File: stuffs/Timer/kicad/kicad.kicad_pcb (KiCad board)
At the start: 2 copper layers, 8 parts, among them SW1 SW_PUSH, SW2 SW_PUSH

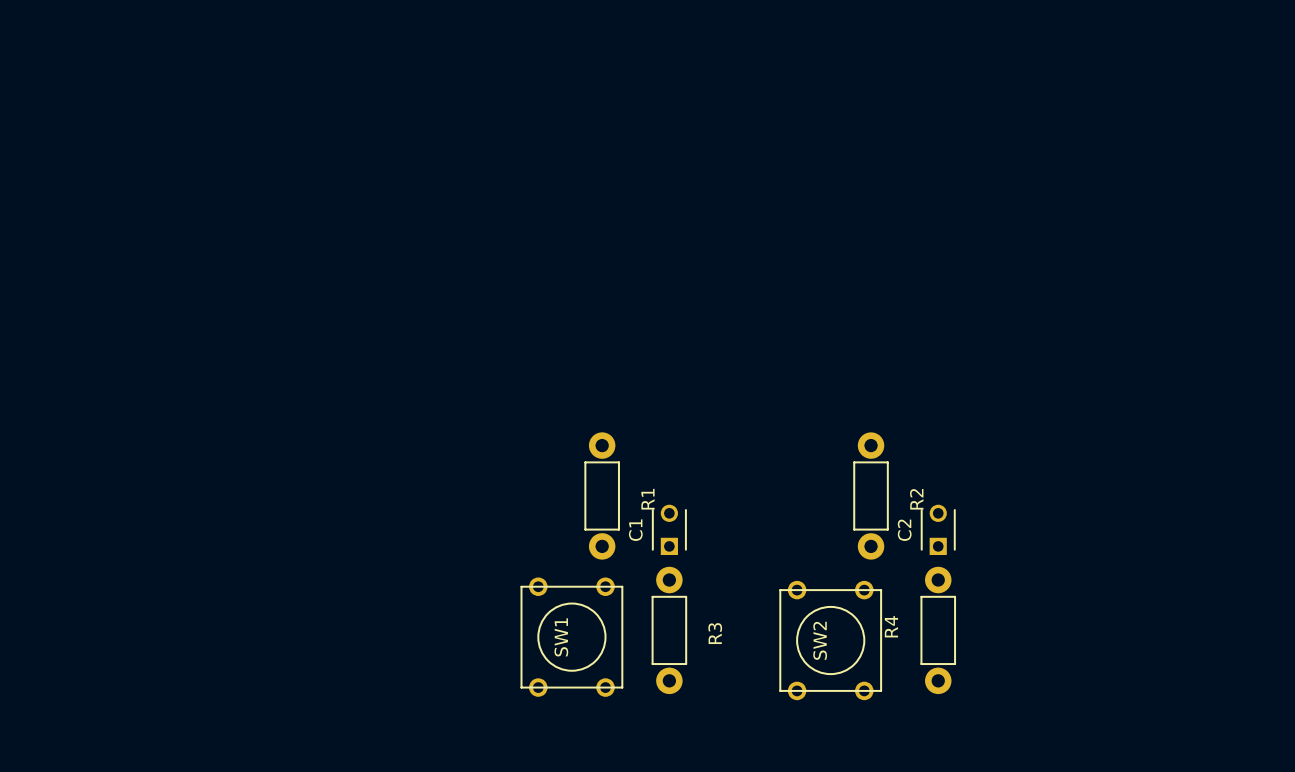
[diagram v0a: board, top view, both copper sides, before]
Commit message: Update kicad files for Timer project.
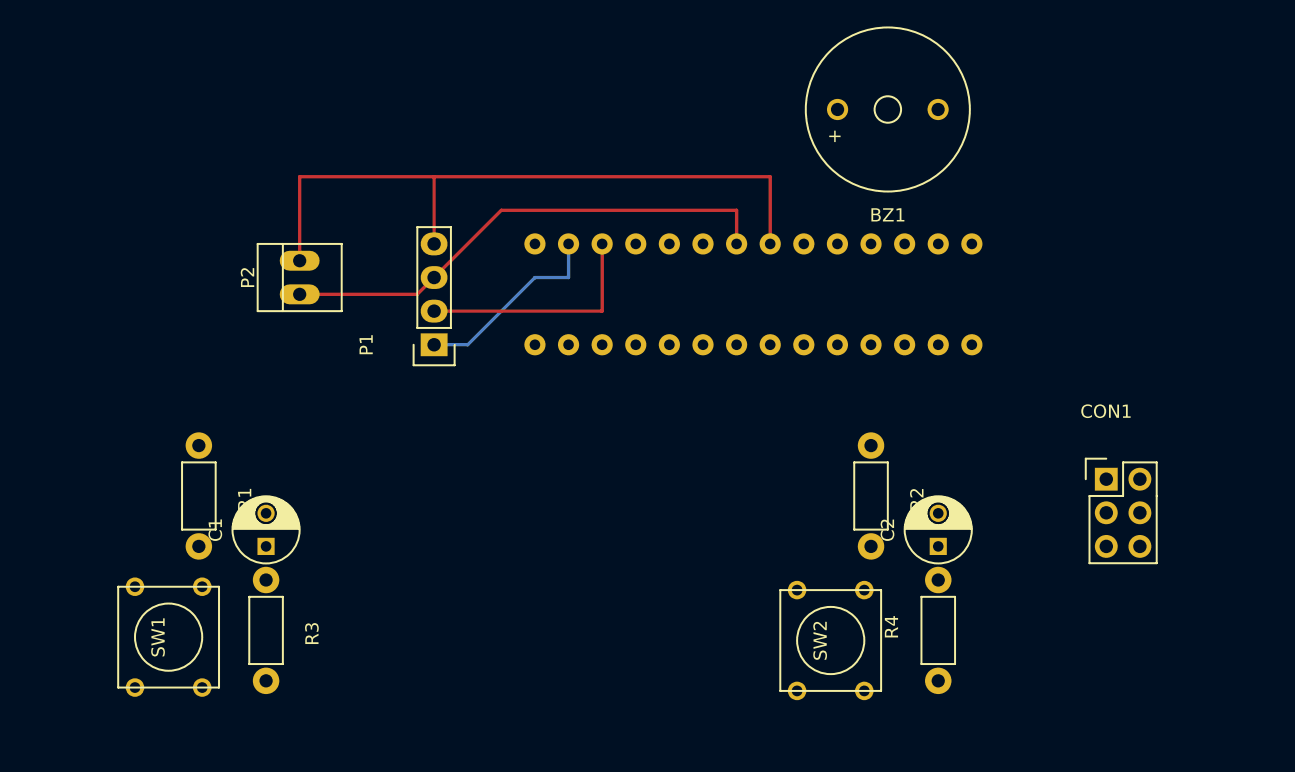
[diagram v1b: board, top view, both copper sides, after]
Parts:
- added BZ1: buzzer, Buzzers_Beepers:MagneticBuzzer_ProSignal_ABI-009-RC, F.Cu at (142.2, 38.1)
- added CON1: AVR-ISP-6, Pin_Headers:Pin_Header_Straight_2x03, F.Cu at (154.9, 66.0)
- added IC1: ATMEGA328P-P, Housings_DIP:DIP-28_W7.62mm, B.Cu at (111.8, 48.3)
- added P1: CONN_01X04, Socket_Strips:Socket_Strip_Straight_1x04, F.Cu at (104.1, 55.9)
- added P2: CONN_01X02, Connect:PINHEAD1-2, F.Cu at (94.0, 50.8)
- C1, C2: footprint Capacitors_ThroughHole:C_Disc_D3_P2.5 -> Capacitors_ThroughHole:C_Radial_D5_L6_P2.5
- moved C1 30.5 mm to (91.4, 71.1)
- moved R1 30.5 mm to (86.4, 63.5)
- moved R3 30.5 mm to (91.4, 73.7)
- moved SW1 30.5 mm to (84.1, 78.0)
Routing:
- net GND: track 0.00 -> 52.1 mm
- net VCC: track 0.00 -> 38.2 mm
- net DISPLAY_IO: track 0.00 -> 17.8 mm
- net DISPLAY_CLK: track 0.00 -> 14.8 mm

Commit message: Update kicad design files.
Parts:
- added C3: 10uF, Capacitors_ThroughHole:C_Radial_D5_L6_P2.5, F.Cu at (121.4, 70.6)
- added R5: 10, Resistors_ThroughHole:Resistor_Horizontal_RM7mm, F.Cu at (115.8, 63.8)
- added R6: 1K, Resistors_ThroughHole:Resistor_Horizontal_RM7mm, F.Cu at (121.4, 73.9)
- added SW3: SW_PUSH, Buttons_Switches_ThroughHole:SW_PUSH_SMALL, F.Cu at (113.3, 77.7)
- C1, R3: moved to B.Cu
- moved BZ1 18.7 mm to (158.0, 48.3), turned to 270 degrees
- moved R4 6.86 mm to (142.2, 74.4), turned to 270 degrees
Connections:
- IC1 pad 11: Net-(IC1-Pad11) -> INCREASE
- IC1 pad 12: Net-(IC1-Pad12) -> DECREASE
- IC1 pad 2: DISPLAY_CLK -> Net-(IC1-Pad2)
- IC1 pad 3: DISPLAY_IO -> Net-(IC1-Pad3)
- IC1 pad 4: PLAY -> DISPLAY_CLK
- IC1 pad 5: Net-(IC1-Pad5) -> DISPLAY_IO
- IC1 pad 6: Net-(IC1-Pad6) -> PLAY
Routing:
- net VCC: track 38.2 -> 185.5 mm
- net GND: track 52.1 -> 164.8 mm
- net Net-(CON1-Pad5): track 0.00 -> 89.8 mm
- net PLAY: track 0.00 -> 45.2 mm
- net DECREASE: track 0.00 -> 37.4 mm, vias 0 -> 1
- net INCREASE: track 0.00 -> 28.3 mm
- net Net-(CON1-Pad3): track 0.00 -> 25.6 mm
- net Net-(CON1-Pad4): track 0.00 -> 25.2 mm
- net Net-(CON1-Pad1): track 0.00 -> 22.0 mm
- net Net-(R2-Pad2): track 0.00 -> 16.7 mm
- net Net-(R1-Pad2): track 0.00 -> 15.8 mm
- net Net-(R5-Pad2): track 0.00 -> 15.7 mm
- net Net-(BZ1-Pad1): track 0.00 -> 13.2 mm
- net DISPLAY_CLK: track 14.8 -> 18.4 mm
- net DISPLAY_IO: track 17.8 -> 19.9 mm
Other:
- board outline added: 93.7 x 43.4 mm
